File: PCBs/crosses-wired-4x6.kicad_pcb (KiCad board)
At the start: 2 copper layers, 202.1 x 133.6 mm, 119 parts, among them J1 Conn_01x14_Pin, J2 Conn_01x04_Socket, J3 Conn_01x14_Pin, J4 Conn_01x04_Socket

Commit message: Removed OLED headers and traces
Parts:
- removed J2, J4: Conn_01x04_Socket, Connector_PinHeader_2.54mm:PinHeader_1x04_P2.54mm_Vertical
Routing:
- net SCL-R: track 45.4 -> 0.00 mm, vias 2 -> 0
- net SDA-R: track 45.4 -> 0.00 mm, vias 2 -> 0
- net SDA: track 38.9 -> 0.00 mm
- net VCC-R: track 38.2 -> 0.00 mm, vias 1 -> 0
- net SCL: track 38.0 -> 0.00 mm
- net VCC: track 30.2 -> 0.00 mm, vias 1 -> 0

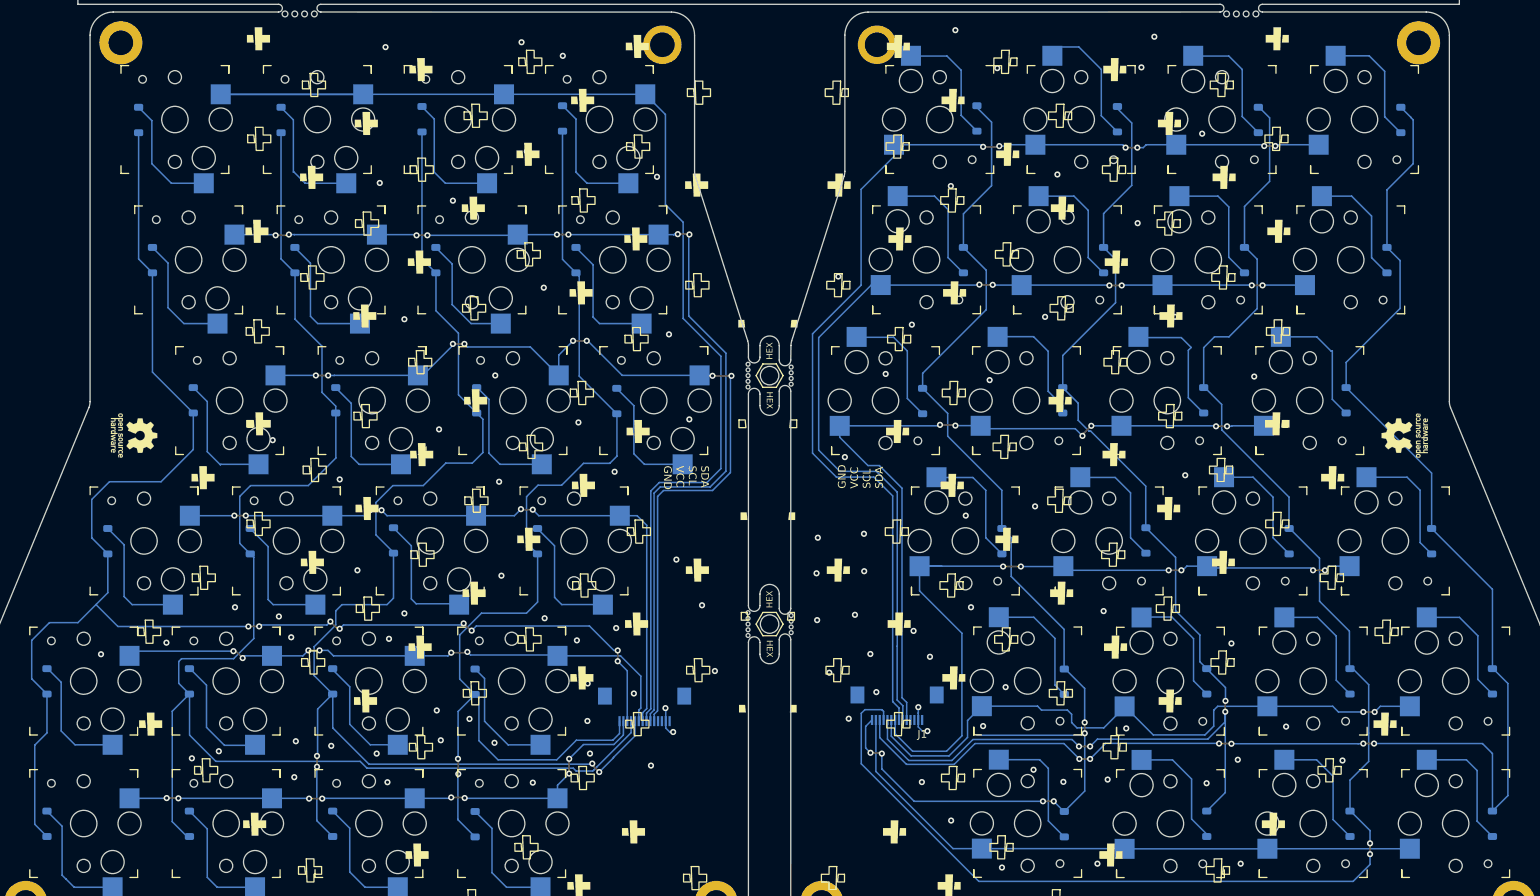
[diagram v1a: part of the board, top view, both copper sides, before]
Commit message: Added schematic | Updated PCB references
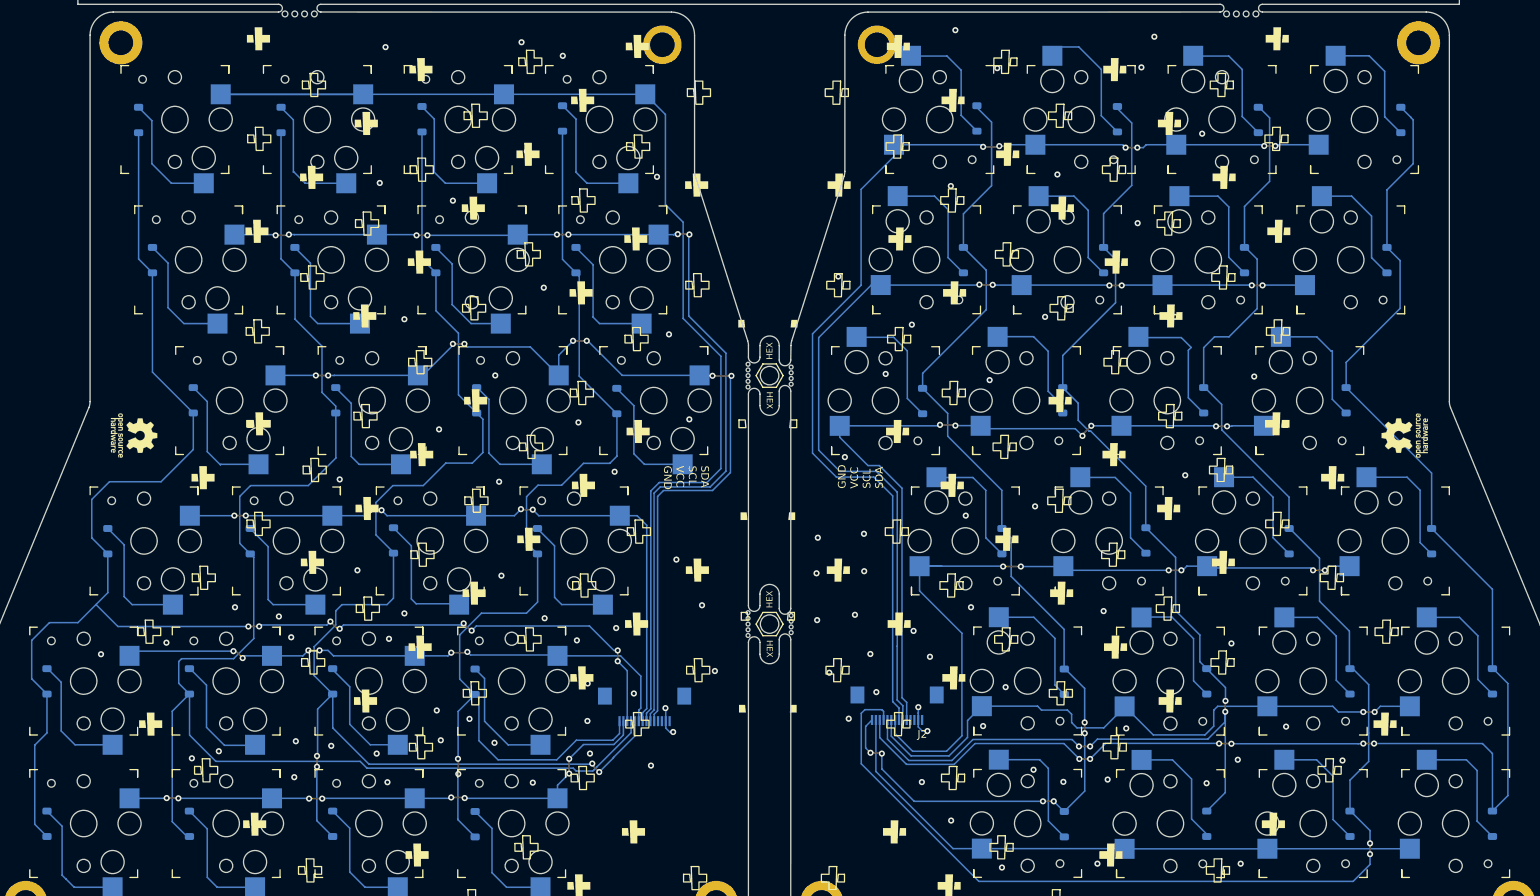
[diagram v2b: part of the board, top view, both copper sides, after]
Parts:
- renumbered D31 to D1, D7 to D10, D12 to D11, D45 to D12, D3 to D13, D8 to D14, D13 to D15, D46 to D16, D4 to D17, D9 to D18, D14 to D19, D32 to D2, D47 to D20, D5 to D21, D10 to D22, D15 to D23, D48 to D24, D34 to D25, D35 to D26, D36 to D27, D37 to D28, D16 to D29, D33 to D3, D21 to D30, D26 to D31, D38 to D32, D17 to D33, D22 to D34, D27 to D35, D39 to D36, D18 to D37, D23 to D38, D28 to D39, D43 to D4, D19 to D41, D24 to D42, D29 to D43, D41 to D44, D20 to D45, D25 to D46, D30 to D47, D42 to D48, D1 to D5, D11 to D7, D44 to D8, D2 to D9, J3 to J1, J1 to J2, CH9 to S18, CH31 to SW1, CH7 to SW10, CH12 to SW11, CH45 to SW12, CH3 to SW13, CH8 to SW14, CH13 to SW15, CH46 to SW16, CH4 to SW17, CH14 to SW19, CH32 to SW2, CH47 to SW20, CH5 to SW21, CH10 to SW22, CH15 to SW23, CH48 to SW24, CH34 to SW25, CH35 to SW26, CH36 to SW27, CH37 to SW28, CH16 to SW29, CH33 to SW3, CH21 to SW30, CH26 to SW31, CH38 to SW32, CH17 to SW33, CH22 to SW34, CH27 to SW35, CH39 to SW36, CH18 to SW37, CH23 to SW38, CH28 to SW39, CH43 to SW4, CH40 to SW40, CH19 to SW41, CH24 to SW42, CH29 to SW43, CH41 to SW44, CH20 to SW45, CH25 to SW46, CH30 to SW47, CH42 to SW48, CH1 to SW5, CH6 to SW6, CH11 to SW7, CH44 to SW8, CH2 to SW9
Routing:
- net R-ROW-N1: track 157.1 -> 142.4 mm
- net Net-(D25-A): track 17.0 -> 15.4 mm
- net R-COL1: track 96.2 -> 95.0 mm
- net L-COL0: track 75.2 -> 74.2 mm
- net R-ROW1: track 200.6 -> 199.6 mm
- net L-COL2: track 120.7 -> 120.1 mm
- net R-COL2: track 99.1 -> 98.5 mm
- net GND: vias 103 -> 102

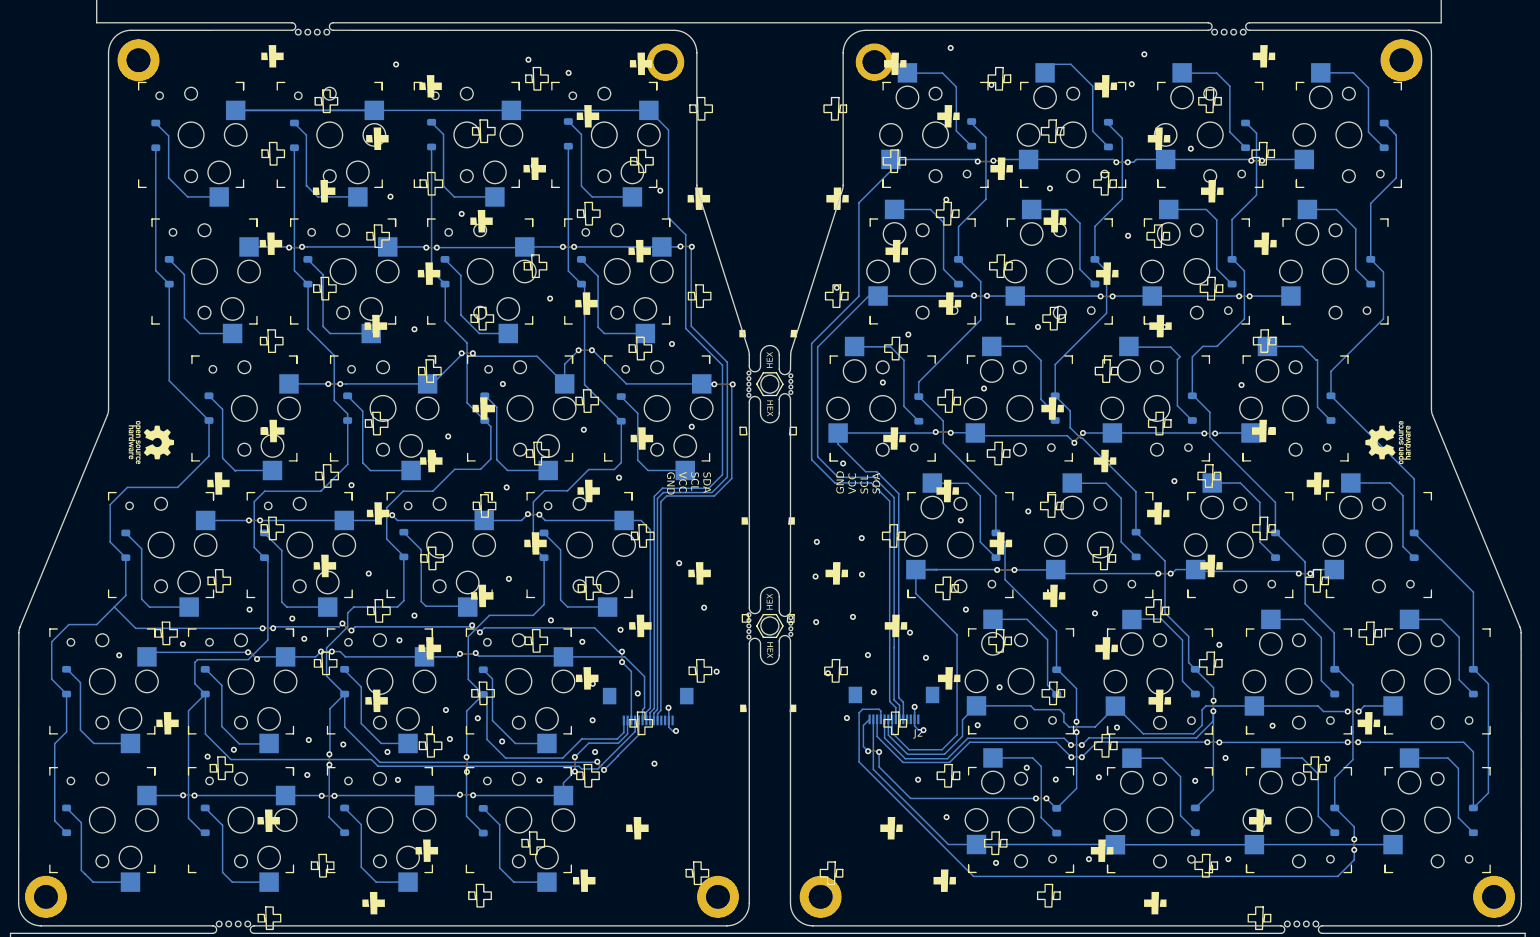
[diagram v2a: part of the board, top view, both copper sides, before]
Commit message: Switched to non-hotswap footprints | Rerouted board for new switch footprints
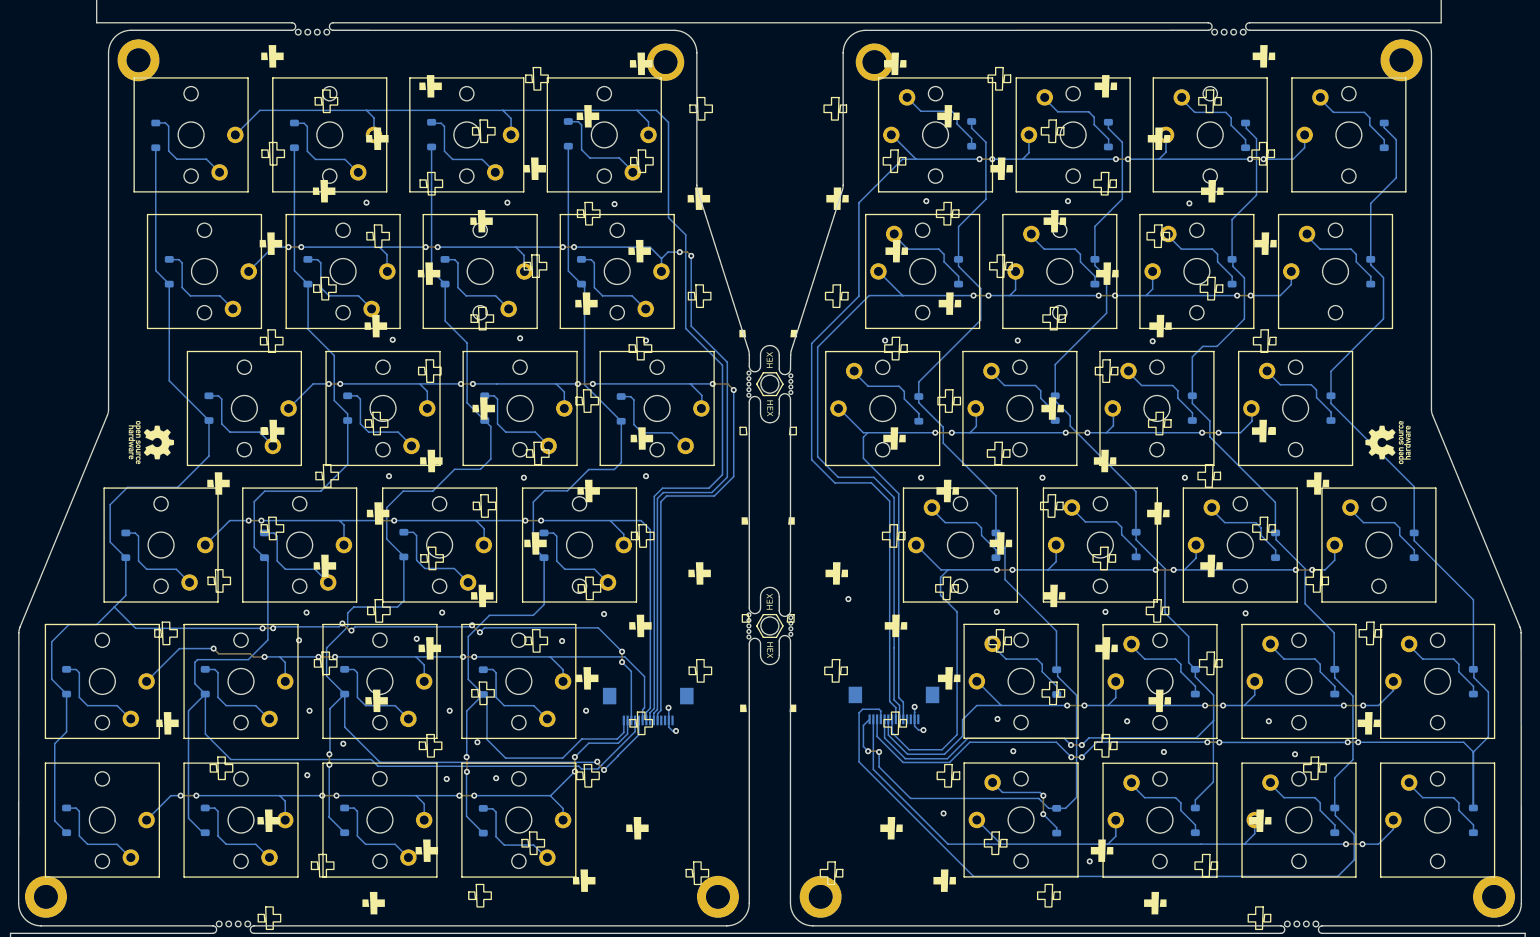
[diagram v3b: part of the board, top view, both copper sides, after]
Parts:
- D1, D10, D11, D12, D13, D14, D15, D16, D17, D18, D19, D2, D20, D21, D22, D23, D24, D25, D26, D27, D28, D29, D3, D30, D31, D32, D33, D34, D35, D36, D37, D38, D39, D4, D40, D41, D42, D43, D44, D45, D46, D47, D48, D5, D6, D7, D8, D9: value 1N4148 -> D
- SW1, SW10, SW11, SW12, SW13, SW14, SW15, SW16, SW17, SW19, SW2, SW20, SW21, SW22, SW23, SW24, SW25, SW26, SW27, SW28, SW29, SW3, SW30, SW31, SW32, SW33, SW34, SW35, SW36, SW37, SW38, SW39, SW4, SW40, SW41, SW42, SW43, SW44, SW45, SW46, SW47, SW48, SW5, SW6, SW7, SW8, SW9: value CPG135001S30 -> SW_Push; footprint keyswitches:Kailh_socket_PG1350 -> PCM_Switch_Keyboard_Kailh:SW_Kailh_Choc_V1
- SW18: renamed from S18; value CPG135001S30 -> SW_Push; footprint keyswitches:Kailh_socket_PG1350 -> PCM_Switch_Keyboard_Kailh:SW_Kailh_Choc_V1
- turned SW1 to -90 degrees
- turned SW10 to -90 degrees
- turned SW11 to -90 degrees
- turned SW12 to -90 degrees
- turned SW13 to -90 degrees
- turned SW14 to -90 degrees
- turned SW15 to -90 degrees
- turned SW16 to -90 degrees
- turned SW17 to -90 degrees
- turned SW18 to -90 degrees
- turned SW19 to -90 degrees
- turned SW2 to -90 degrees
- turned SW20 to -90 degrees
- turned SW21 to -90 degrees
- turned SW22 to -90 degrees
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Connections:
- net L-COL0 renamed /L-COL0
- net L-COL1 renamed /L-COL1
- net L-COL2 renamed /L-COL2
- net L-COL3 renamed /L-COL3
- net L-COL4 renamed /L-COL4
- net L-COLP renamed /L-COLP
- net L-ROW-N1 renamed /L-ROW-N1
- net L-ROW0 renamed /L-ROW0
- net L-ROW1 renamed /L-ROW1
- net L-ROW2 renamed /L-ROW2
- net R-COL0 renamed /R-COL0
- net R-COL1 renamed /R-COL1
- net R-COL2 renamed /R-COL2
- net R-COL3 renamed /R-COL3
- net R-COL4 renamed /R-COL4
- net R-COLP renamed /R-COLP
- net R-ROW-N1 renamed /R-ROW-N1
- net R-ROW0 renamed /R-ROW0
- net R-ROW1 renamed /R-ROW1
- net R-ROW2 renamed /R-ROW2
- J1 pad 11: SDA -> unconnected-(J1-Pin_11-Pad11)
- J1 pad 12: SCL -> unconnected-(J1-Pin_12-Pad12)
- J1 pad 14: VCC -> unconnected-(J1-Pin_14-Pad14)
- J2 pad 11: SDA-R -> unconnected-(J2-Pin_11-Pad11)
- J2 pad 12: SCL-R -> unconnected-(J2-Pin_12-Pad12)
- J2 pad 14: VCC-R -> unconnected-(J2-Pin_14-Pad14)
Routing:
- net /R-COLP: track 80.1 -> 94.3 mm, vias 0 -> 2
- net /R-COL3: track 123.1 -> 137.0 mm
- net /L-COL4: track 148.2 -> 161.6 mm
- net /L-COL0: track 74.2 -> 87.1 mm
- net /R-COL4: track 142.4 -> 155.1 mm
- net /L-COLP: track 71.6 -> 83.1 mm
- net /L-COL1: track 86.8 -> 98.1 mm
- net /L-COL3: track 132.3 -> 142.7 mm
- net /R-COL2: track 98.5 -> 106.7 mm
- net /R-COL1: track 95.0 -> 103.1 mm
- net /R-COL0: track 82.3 -> 88.6 mm, vias 2 -> 6
- net /L-COL2: track 120.1 -> 124.4 mm
- net Net-(D39-A): track 16.8 -> 12.5 mm
- net Net-(D36-A): track 16.5 -> 12.5 mm
- net Net-(D28-A): track 16.5 -> 12.5 mm
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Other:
- board text removed: "GND VCC SCL SDA"
- board text removed: "SDA SCL VCC GND"
